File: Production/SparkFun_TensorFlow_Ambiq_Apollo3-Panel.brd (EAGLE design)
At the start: 162.4 x 134.7 mm, 1077 parts, among them J14 CORTEX_DEBUG_PTH, J15 CAMERA-0V7670, J20 CORTEX_DEBUG_PTH, J21 CAMERA-0V7670, J26 CORTEX_DEBUG_PTH, J27 CAMERA-0V7670, J32 CORTEX_DEBUG_PTH, J33 CAMERA-0V7670, J38 CORTEX_DEBUG_PTH, J39 CAMERA-0V7670, J44 CORTEX_DEBUG_PTH, J45 CAMERA-0V7670, J5 CORTEX_DEBUG_PTH, J50 CORTEX_DEBUG_PTH, J51 CAMERA-0V7670, J6 CAMERA-0V7670, J8 CORTEX_DEBUG_PTH, J9 CAMERA-0V7670, M1 MEMS_MIC, M10 MEMS_MIC, M11 MEMS_MIC, M12 MEMS_MIC, M13 MEMS_MIC, M14 MEMS_MIC, M15 MEMS_MIC, M16 MEMS_MIC, M17 MEMS_MIC, M18 MEMS_MIC, M2 MEMS_MIC, M3 MEMS_MIC, M4 MEMS_MIC, M5 MEMS_MIC, M6 MEMS_MIC, M7 MEMS_MIC, M8 MEMS_MIC, M9 MEMS_MIC, U1 AMBIQ-APOLLO3KBR, U10 LIS2DH12, U11 1.8V, U12 LMV358, U13 AMBIQ-APOLLO3KBR, U14 LIS2DH12, U15 1.8V, U16 LMV358, U17 AMBIQ-APOLLO3KBR, U18 LIS2DH12, U19 1.8V, U2 LIS2DH12, U20 LMV358, U21 AMBIQ-APOLLO3KBR, U22 LIS2DH12, U23 1.8V, U24 LMV358, U25 AMBIQ-APOLLO3KBR, U26 LIS2DH12, U27 1.8V, U28 LMV358, U29 AMBIQ-APOLLO3KBR, U3 1.8V, U30 LIS2DH12, U31 1.8V, U32 LMV358, U33 AMBIQ-APOLLO3KBR, U34 LIS2DH12, U35 1.8V, U36 LMV358, U4 LMV358, U5 AMBIQ-APOLLO3KBR, U6 LIS2DH12, U7 1.8V, U8 LMV358, U9 AMBIQ-APOLLO3KBR, Y1 32MHz, Y10 32.768kHz, Y11 32MHz, Y12 32.768kHz, Y13 32MHz, Y14 32.768kHz, Y15 32MHz, Y16 32.768kHz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

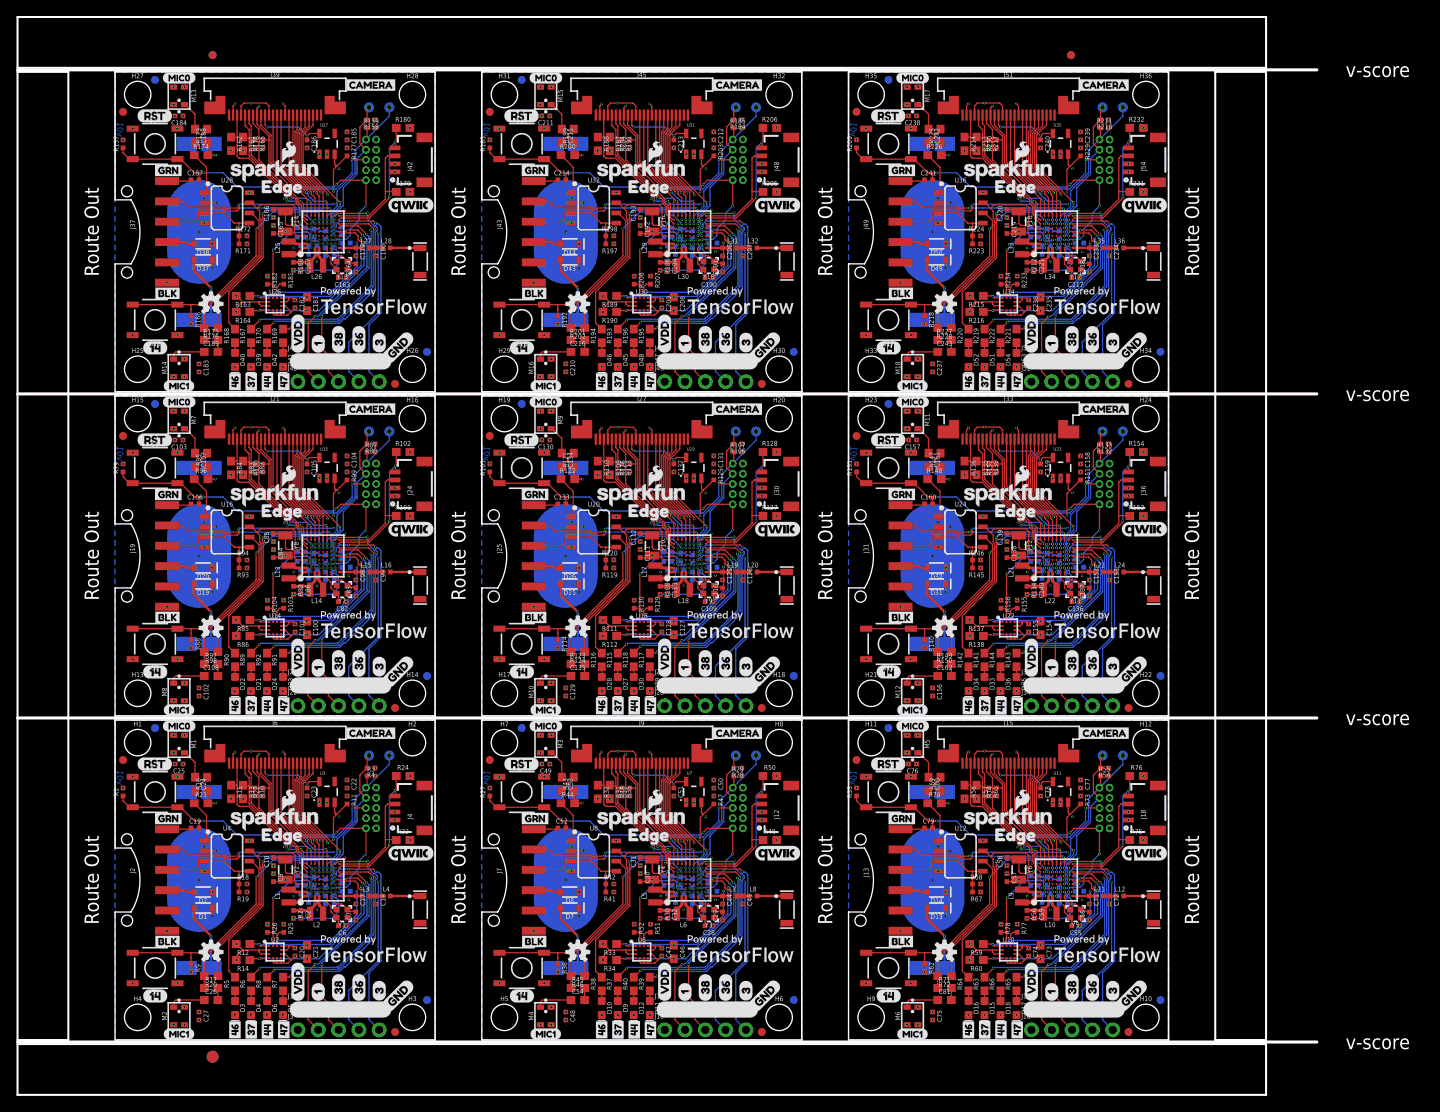
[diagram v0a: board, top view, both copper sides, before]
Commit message: Adding v01 Production panel.
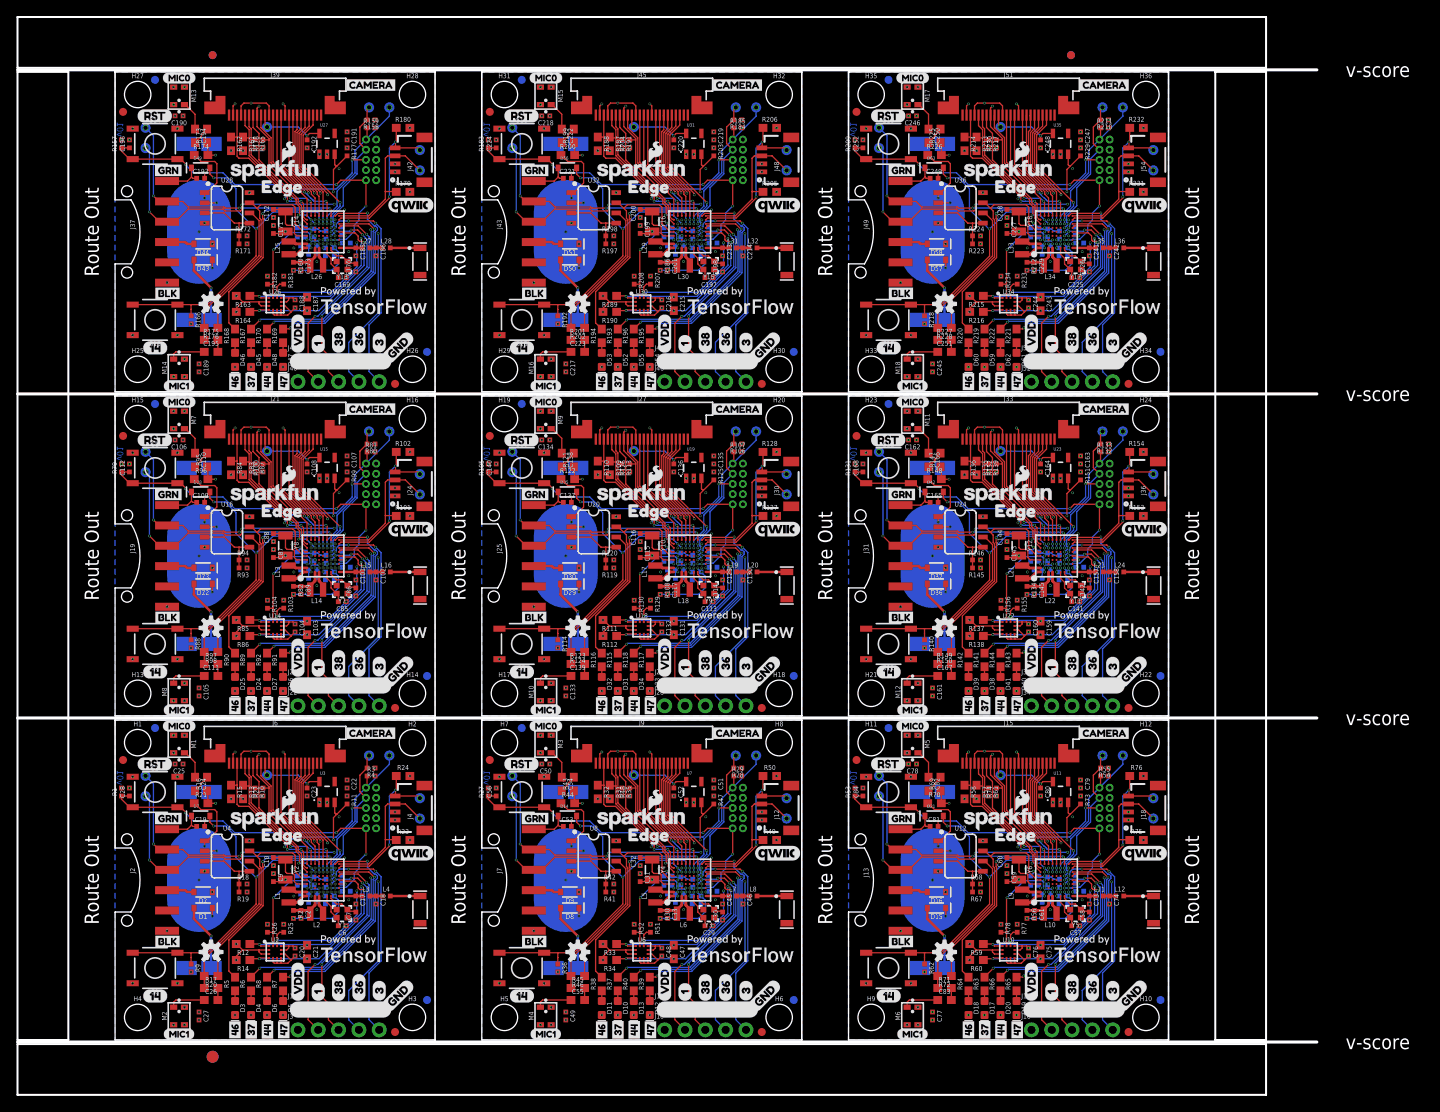
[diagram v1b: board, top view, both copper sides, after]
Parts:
- added C244, C245, C246, C249: 0.1uF, ambiq:0402-TIGHT
- added C247, C248: 1.0uF, ambiq:0402-TIGHT
- added C250, C251: 4.7uF, SparkFun-Capacitors:0603
- added C252: 1.0nF, ambiq:0402-TIGHT
- added D55, D62: GREEN, SparkFun-LED:LED-0603
- added D56, D63: 250mA/100V, SparkFun-DiscreteSemi:SOD-323
- added D57, D58: 1A/23V/620mV, SparkFun-DiscreteSemi:SOD-323@1
- added D59: BLUE, SparkFun-LED:LED-0603
- added D60: RED, SparkFun-LED:LED-0603
- added D61: Yellow, SparkFun-LED:LED-0603
- added TP19, TP20, TP21, TP22, TP23, TP24, TP25, TP26, TP27, TP28, TP29, TP30, TP31, TP32, TP33, TP34, TP35, TP36, TP37, TP38, TP39, TP40, TP41, TP42, TP43, TP44, TP45, TP46, TP47, TP48, TP49, TP50, TP51, TP52, TP53, TP54, TP55, TP56, TP57, TP58, TP59, TP60, TP61, TP62, TP63: TEST-POINT3X5, SparkFun-Connectors:PAD.03X.05
- added U$235, U$265: (no value), buzzard_labels:MIC00
- added U$236, U$266: (no value), buzzard_labels:MIC11
- added U$237, U$264, U$267: (no value), buzzard_labels:EDGE0
- added U$238, U$263, U$268: (no value), PoweredBy_TF#jpg:POWEREDBY_TF#JPG
- added U$239, U$269: (no value), SparkFun-Aesthetics:SFE_LOGO_NAME_.1
- added U$240, U$270: (no value), SparkFun-Aesthetics:OSHW-LOGO-S
- added U$241, U$248: (no value), buzzard_labels:GND0
- added U$242, U$245: (no value), buzzard_labels:VDD1
- added U$243, U$246: (no value), buzzard_labels:383
- added U$244, U$247: (no value), buzzard_labels:364
- added U$249: (no value), buzzard_labels:1416
- added U$250: (no value), buzzard_labels:RST15
- added U$251: (no value), buzzard_labels:BLK2
- added U$252: (no value), buzzard_labels:GRN1
- added U$253, U$254: (no value), buzzard_labels:10
- added U$255, U$256: (no value), buzzard_labels:31
- added U$257: (no value), buzzard_labels:461
- added U$258: (no value), buzzard_labels:372
- added U$259: (no value), buzzard_labels:443
- added U$260: (no value), buzzard_labels:470
- added U$261: (no value), Labels:QWIIC_COPYRIGHT_SMALL
- added U$262: (no value), buzzard_labels:CAMERA3
- BT1, BT2, BT3, BT4, BT5, BT6, BT7, BT8, BT9: device SparkFun-Batteries:BATTCON_20MM_4LEGS_OVERPASTE -> SparkFun-Batteries:BATTCON_20MM_4LEGS_OVERPASTE_INNER
- C100: value 10uF -> 2.2uF; device SparkFun-Capacitors:0603 -> ambiq:0402-TIGHT
- C101, C129, C157, C241: value 0.1uF -> DNP
- C102, C130, C214, C74: value 0.1uF -> 0.5pF
- C103, C187, C47, C75: value 0.1uF -> 10uF; device ambiq:0402-TIGHT -> SparkFun-Capacitors:0603
- C104, C105, C132, C50, C77, C78: value 1.0uF -> 0.1uF
- C107, C108, C135, C80: value 4.7uF -> 1.0uF; device SparkFun-Capacitors:0603 -> ambiq:0402-TIGHT
- C109, C137, C190, C217, C218: value 6pF -> 0.1uF
- C110, C55, C82, C83: value 6pF -> 4.7uF; device ambiq:0402-TIGHT -> SparkFun-Capacitors:0603
- C111, C138, C139, C166: value 15pF -> 4.7uF; device ambiq:0402-TIGHT -> SparkFun-Capacitors:0603
- C112, C84: value 15pF -> 1.0nF
- C113, C86: value 4.7uF -> 6pF
- C114, C141: value 1.0uF -> 6pF
- C115, C88: value 0.47uF -> 15pF
- C116, C143, C144, C171, C172, C199: value 2.2uF -> 15pF
- C117, C145, C89: value 2.2uF -> 4.7uF
- C118, C124, C151, C62, C70, C90, C97: value 2.2uF -> 1.0uF
- C119, C147, C175, C203: value 1.0uF -> 0.47uF
- C120, C121, C122, C148, C149, C176, C212, C240, C38, C65, C66, C92, C93, C94: value 1.0uF -> 2.2uF
- C123, C42, C69, C96: value 47nF -> 1.0uF
- C125, C152, C179, C98: value DNP -> 1.0uF
- C126, C153, C180, C207: value 0.5pF -> 1.0uF
- C127: value 10uF -> 47nF; device SparkFun-Capacitors:0603 -> ambiq:0402-TIGHT
- C128, C156, C184: value 0.1uF -> 2.2uF
- C131, C159: value 1.0uF -> 10uF; device ambiq:0402-TIGHT -> SparkFun-Capacitors:0603
- C134, C161, C162, C188, C189, C216, C53, C81: value 4.7uF -> 0.1uF; device SparkFun-Capacitors:0603 -> ambiq:0402-TIGHT
- C136, C163, C164, C191: value 6pF -> 1.0uF
- C140: value 4.7uF -> 1.0nF
- C142, C169: value 0.47uF -> 6pF
- C150, C177, C204: value 47nF -> 2.2uF
- C154, C181, C208, C235: value 10uF -> 1.0uF; device SparkFun-Capacitors:0603 -> ambiq:0402-TIGHT
- C155, C183, C211: value 0.1uF -> 47nF
- C158, C186: value 1.0uF -> 0.5pF
- C165, C193: value 15pF -> 0.1uF
- C167, C194: device ambiq:0402-TIGHT -> SparkFun-Capacitors:0603
- C168: value 1.0uF -> 1.0nF
- C170, C197, C198, C225, C226: value 2.2uF -> 6pF
- C173, C201, C229, C33: value 1.0uF -> 4.7uF
- C182, C209, C210, C236, C237, C238, C52, C79: value 0.1uF -> 1.0uF
- C185, C213: value 1.0uF -> DNP
- C192, C219, C220: value 15pF -> 1.0uF
- C195, C222: value 1.0uF -> 4.7uF; device ambiq:0402-TIGHT -> SparkFun-Capacitors:0603
- C196: value 0.47uF -> 1.0nF
- C200, C227, C228, C60, C87: value 1.0uF -> 15pF
- C206, C233, C44: value DNP -> 2.2uF
- C215, C243: value 4.7uF -> 10uF
- C221: value 4.7uF -> 0.1uF
- C223: value 0.47uF -> 4.7uF; device ambiq:0402-TIGHT -> SparkFun-Capacitors:0603
- C224: value 2.2uF -> 1.0nF
- C231: value 47nF -> 0.47uF
- C234, C72: value 0.5pF -> 2.2uF
- C239: value 1.0uF -> 47nF
- C242: value 4.7uF -> 0.5pF; device SparkFun-Capacitors:0603 -> ambiq:0402-TIGHT
- C28, C56: value 6pF -> 1.0nF
- C30, C57, C58, C85: value 15pF -> 6pF
- C32, C59: value 4.7uF -> 15pF
- C34: value 0.47uF -> 1.0uF
- C35, C63, C91: value 2.2uF -> 0.47uF
- C43: value 2.2uF -> 47nF
- C45: value 0.5pF -> DNP
- C46: value 10uF -> 0.5pF; device SparkFun-Capacitors:0603 -> ambiq:0402-TIGHT
- C61: value 0.47uF -> 4.7uF
- C71: value DNP -> 47nF
- C73: value 10uF -> DNP; device SparkFun-Capacitors:0603 -> ambiq:0402-TIGHT
- C99: value 0.5pF -> 47nF
- D1, D2, D37, D43, D44, D50, D8: device SparkFun-DiscreteSemi:SOD-323 -> SparkFun-DiscreteSemi:SOD-323@1
- D10, D52: value RED -> BLUE
- D11, D53: value Yellow -> RED
- D12, D54: value GREEN -> Yellow
- D13, D20: value 1A/23V/620mV -> GREEN; device SparkFun-DiscreteSemi:SOD-323 -> SparkFun-LED:LED-0603
- D14, D49, D7: value 1A/23V/620mV -> 250mA/100V
- D15, D51, D9: value BLUE -> 1A/23V/620mV; device SparkFun-LED:LED-0603 -> SparkFun-DiscreteSemi:SOD-323@1
- D16, D22: value RED -> 1A/23V/620mV; device SparkFun-LED:LED-0603 -> SparkFun-DiscreteSemi:SOD-323@1
- D17: value Yellow -> BLUE
- D18: value GREEN -> RED
- D19, D26: value 1A/23V/620mV -> Yellow; device SparkFun-DiscreteSemi:SOD-323 -> SparkFun-LED:LED-0603
- D21: value BLUE -> 250mA/100V; device SparkFun-LED:LED-0603 -> SparkFun-DiscreteSemi:SOD-323
- D23, D29: value Yellow -> 1A/23V/620mV; device SparkFun-LED:LED-0603 -> SparkFun-DiscreteSemi:SOD-323@1
- D24: value GREEN -> BLUE
- D25, D32: value 1A/23V/620mV -> RED; device SparkFun-DiscreteSemi:SOD-323 -> SparkFun-LED:LED-0603
- D27: value BLUE -> GREEN
- D28: value RED -> 250mA/100V; device SparkFun-LED:LED-0603 -> SparkFun-DiscreteSemi:SOD-323
- D30, D36: value GREEN -> 1A/23V/620mV; device SparkFun-LED:LED-0603 -> SparkFun-DiscreteSemi:SOD-323@1
- D31, D38: value 1A/23V/620mV -> BLUE; device SparkFun-DiscreteSemi:SOD-323 -> SparkFun-LED:LED-0603
- D33: value BLUE -> Yellow
- D34: value RED -> GREEN
- D35: value Yellow -> 250mA/100V; device SparkFun-LED:LED-0603 -> SparkFun-DiscreteSemi:SOD-323
- D39: value BLUE -> RED
- D40: value RED -> Yellow
- D41: value Yellow -> GREEN
- D42: value GREEN -> 250mA/100V; device SparkFun-LED:LED-0603 -> SparkFun-DiscreteSemi:SOD-323
- R120, R146, R172, R18, R198, R224, R42, R68, R94: value 10k -> 22k
- U$100: device buzzard_labels:CAMERA3 -> buzzard_labels:RST15
- U$101: device PoweredBy_TF#jpg:POWEREDBY_TF#JPG -> buzzard_labels:BLK2
- U$102: device buzzard_labels:EDGE0 -> buzzard_labels:GRN1
- U$103: device buzzard_labels:MIC00 -> buzzard_labels:10
- U$104: device buzzard_labels:MIC11 -> buzzard_labels:10
- U$105: device buzzard_labels:GND0 -> buzzard_labels:31
- U$106, U$135: device buzzard_labels:VDD1 -> buzzard_labels:31
- U$107: device buzzard_labels:383 -> buzzard_labels:461
- U$108: device buzzard_labels:364 -> buzzard_labels:372
- U$109: device buzzard_labels:VDD1 -> buzzard_labels:443
- U$110: device buzzard_labels:383 -> buzzard_labels:470
- U$111: device buzzard_labels:364 -> Labels:QWIIC_COPYRIGHT_SMALL
- U$112: device buzzard_labels:GND0 -> buzzard_labels:CAMERA3
- U$113: device buzzard_labels:1416 -> PoweredBy_TF#jpg:POWEREDBY_TF#JPG
- U$114: device buzzard_labels:RST15 -> buzzard_labels:EDGE0
- U$115: device buzzard_labels:BLK2 -> buzzard_labels:MIC00
- U$116: device buzzard_labels:GRN1 -> buzzard_labels:MIC11
- U$117, U$144: device buzzard_labels:10 -> buzzard_labels:EDGE0
- U$118, U$143: device buzzard_labels:10 -> PoweredBy_TF#jpg:POWEREDBY_TF#JPG
- U$119: device buzzard_labels:31 -> SparkFun-Aesthetics:SFE_LOGO_NAME_.1
- U$120: device buzzard_labels:31 -> SparkFun-Aesthetics:OSHW-LOGO-S
- U$121: device buzzard_labels:461 -> buzzard_labels:GND0
- U$122: device buzzard_labels:372 -> buzzard_labels:VDD1
- U$123: device buzzard_labels:443 -> buzzard_labels:383
- U$124: device buzzard_labels:470 -> buzzard_labels:364
- U$125: device Labels:QWIIC_COPYRIGHT_SMALL -> buzzard_labels:VDD1
- U$126: device buzzard_labels:CAMERA3 -> buzzard_labels:383
- U$127: device PoweredBy_TF#jpg:POWEREDBY_TF#JPG -> buzzard_labels:364
- U$128: device buzzard_labels:EDGE0 -> buzzard_labels:GND0
- U$129: device buzzard_labels:MIC00 -> buzzard_labels:1416
- U$130: device buzzard_labels:MIC11 -> buzzard_labels:RST15
- U$131: device buzzard_labels:GND0 -> buzzard_labels:BLK2
- U$132: device buzzard_labels:VDD1 -> buzzard_labels:GRN1
- U$133: device buzzard_labels:383 -> buzzard_labels:10
- U$134, U$163: device buzzard_labels:364 -> buzzard_labels:10
- U$136: device buzzard_labels:383 -> buzzard_labels:31
- U$137: device buzzard_labels:364 -> buzzard_labels:461
- U$138: device buzzard_labels:GND0 -> buzzard_labels:372
- U$139: device buzzard_labels:1416 -> buzzard_labels:443
- U$140: device buzzard_labels:RST15 -> buzzard_labels:470
- U$141: device buzzard_labels:BLK2 -> Labels:QWIIC_COPYRIGHT_SMALL
- U$142: device buzzard_labels:GRN1 -> buzzard_labels:CAMERA3
- U$145: device buzzard_labels:31 -> buzzard_labels:MIC00
- U$146: device buzzard_labels:31 -> buzzard_labels:MIC11
- U$147: device buzzard_labels:461 -> buzzard_labels:EDGE0
- U$148: device buzzard_labels:372 -> PoweredBy_TF#jpg:POWEREDBY_TF#JPG
- U$149: device buzzard_labels:443 -> SparkFun-Aesthetics:SFE_LOGO_NAME_.1
- U$150: device buzzard_labels:470 -> SparkFun-Aesthetics:OSHW-LOGO-S
- U$151: device Labels:QWIIC_COPYRIGHT_SMALL -> buzzard_labels:GND0
- U$152: device buzzard_labels:CAMERA3 -> buzzard_labels:VDD1
- U$153: device PoweredBy_TF#jpg:POWEREDBY_TF#JPG -> buzzard_labels:383
- U$154: device buzzard_labels:EDGE0 -> buzzard_labels:364
- U$155: device buzzard_labels:MIC00 -> buzzard_labels:VDD1
- U$156: device buzzard_labels:MIC11 -> buzzard_labels:383
- U$157, U$34: device buzzard_labels:GND0 -> buzzard_labels:364
- U$158, U$31: device buzzard_labels:VDD1 -> buzzard_labels:GND0
- U$159: device buzzard_labels:383 -> buzzard_labels:1416
- U$160: device buzzard_labels:364 -> buzzard_labels:RST15
- U$161: device buzzard_labels:VDD1 -> buzzard_labels:BLK2
- U$162: device buzzard_labels:383 -> buzzard_labels:GRN1
- U$164: device buzzard_labels:GND0 -> buzzard_labels:10
- U$165: device buzzard_labels:1416 -> buzzard_labels:31
- U$166: device buzzard_labels:RST15 -> buzzard_labels:31
- U$167: device buzzard_labels:BLK2 -> buzzard_labels:461
- U$168: device buzzard_labels:GRN1 -> buzzard_labels:372
- U$169: device buzzard_labels:10 -> buzzard_labels:443
- U$170: device buzzard_labels:10 -> buzzard_labels:470
- U$171: device buzzard_labels:31 -> Labels:QWIIC_COPYRIGHT_SMALL
- U$172: device buzzard_labels:31 -> buzzard_labels:CAMERA3
- U$173: device buzzard_labels:461 -> PoweredBy_TF#jpg:POWEREDBY_TF#JPG
- U$174: device buzzard_labels:372 -> buzzard_labels:EDGE0
- U$175: device buzzard_labels:443 -> buzzard_labels:MIC00
- U$176: device buzzard_labels:470 -> buzzard_labels:MIC11
- U$177: device Labels:QWIIC_COPYRIGHT_SMALL -> buzzard_labels:EDGE0
- U$178: device buzzard_labels:CAMERA3 -> PoweredBy_TF#jpg:POWEREDBY_TF#JPG
- U$179: device PoweredBy_TF#jpg:POWEREDBY_TF#JPG -> SparkFun-Aesthetics:SFE_LOGO_NAME_.1
- U$180: device buzzard_labels:EDGE0 -> SparkFun-Aesthetics:OSHW-LOGO-S
- U$181: device buzzard_labels:MIC00 -> buzzard_labels:GND0
- U$182: device buzzard_labels:MIC11 -> buzzard_labels:VDD1
- U$183, U$216: device buzzard_labels:GND0 -> buzzard_labels:383
- U$184, U$187: device buzzard_labels:VDD1 -> buzzard_labels:364
- U$185, U$32: device buzzard_labels:383 -> buzzard_labels:VDD1
- U$186, U$33: device buzzard_labels:364 -> buzzard_labels:383
- U$188, U$211: device buzzard_labels:383 -> buzzard_labels:GND0
- U$189: device buzzard_labels:364 -> buzzard_labels:1416
- U$190: device buzzard_labels:GND0 -> buzzard_labels:RST15
- U$191: device buzzard_labels:1416 -> buzzard_labels:BLK2
- U$192: device buzzard_labels:RST15 -> buzzard_labels:GRN1
- U$193: device buzzard_labels:BLK2 -> buzzard_labels:10
- U$194: device buzzard_labels:GRN1 -> buzzard_labels:10
- U$195, U$196: device buzzard_labels:10 -> buzzard_labels:31
- U$197: device buzzard_labels:31 -> buzzard_labels:461
- U$198: device buzzard_labels:31 -> buzzard_labels:372
- U$199: device buzzard_labels:461 -> buzzard_labels:443
- U$200: device buzzard_labels:372 -> buzzard_labels:470
- U$201: device buzzard_labels:443 -> Labels:QWIIC_COPYRIGHT_SMALL
- U$202: device buzzard_labels:470 -> buzzard_labels:CAMERA3
- U$203: device Labels:QWIIC_COPYRIGHT_SMALL -> PoweredBy_TF#jpg:POWEREDBY_TF#JPG
- U$204: device buzzard_labels:CAMERA3 -> buzzard_labels:EDGE0
- U$205: device PoweredBy_TF#jpg:POWEREDBY_TF#JPG -> buzzard_labels:MIC00
- U$206: device buzzard_labels:EDGE0 -> buzzard_labels:MIC11
- U$207: device buzzard_labels:MIC00 -> buzzard_labels:EDGE0
- U$208: device buzzard_labels:MIC11 -> PoweredBy_TF#jpg:POWEREDBY_TF#JPG
- U$209: device buzzard_labels:GND0 -> SparkFun-Aesthetics:SFE_LOGO_NAME_.1
- U$210: device buzzard_labels:VDD1 -> SparkFun-Aesthetics:OSHW-LOGO-S
- U$212, U$215: device buzzard_labels:364 -> buzzard_labels:VDD1
- U$213: device buzzard_labels:VDD1 -> buzzard_labels:383
- U$214: device buzzard_labels:383 -> buzzard_labels:364
- U$217: device buzzard_labels:1416 -> buzzard_labels:364
- U$218: device buzzard_labels:RST15 -> buzzard_labels:GND0
- U$219: device buzzard_labels:BLK2 -> buzzard_labels:1416
- U$220: device buzzard_labels:GRN1 -> buzzard_labels:RST15
- U$221: device buzzard_labels:10 -> buzzard_labels:BLK2
- U$222: device buzzard_labels:10 -> buzzard_labels:GRN1
- U$223, U$224: device buzzard_labels:31 -> buzzard_labels:10
- U$225: device buzzard_labels:461 -> buzzard_labels:31
- U$226: device buzzard_labels:372 -> buzzard_labels:31
- U$227: device buzzard_labels:443 -> buzzard_labels:461
- U$228: device buzzard_labels:470 -> buzzard_labels:372
- U$229: device Labels:QWIIC_COPYRIGHT_SMALL -> buzzard_labels:443
- U$23: device buzzard_labels:GND0 -> buzzard_labels:EDGE0
- U$230: device buzzard_labels:CAMERA3 -> buzzard_labels:470
- U$231: device PoweredBy_TF#jpg:POWEREDBY_TF#JPG -> Labels:QWIIC_COPYRIGHT_SMALL
- U$232: device buzzard_labels:EDGE0 -> buzzard_labels:CAMERA3
- U$233: device buzzard_labels:MIC00 -> PoweredBy_TF#jpg:POWEREDBY_TF#JPG
- U$234: device buzzard_labels:MIC11 -> buzzard_labels:EDGE0
- U$25, U$83: device buzzard_labels:VDD1 -> PoweredBy_TF#jpg:POWEREDBY_TF#JPG
- U$29: device buzzard_labels:383 -> SparkFun-Aesthetics:SFE_LOGO_NAME_.1
- U$30: device buzzard_labels:364 -> SparkFun-Aesthetics:OSHW-LOGO-S
- U$35: device buzzard_labels:1416 -> buzzard_labels:VDD1
- U$36: device buzzard_labels:RST15 -> buzzard_labels:383
- U$37: device buzzard_labels:BLK2 -> buzzard_labels:364
- U$38: device buzzard_labels:GRN1 -> buzzard_labels:GND0
- U$39: device buzzard_labels:10 -> buzzard_labels:1416
- U$40: device buzzard_labels:10 -> buzzard_labels:RST15
- U$41: device buzzard_labels:31 -> buzzard_labels:BLK2
- U$42: device buzzard_labels:31 -> buzzard_labels:GRN1
- U$43: device buzzard_labels:461 -> buzzard_labels:10
- U$44: device buzzard_labels:372 -> buzzard_labels:10
- U$45: device buzzard_labels:443 -> buzzard_labels:31
- U$46: device buzzard_labels:470 -> buzzard_labels:31
- U$47: device Labels:QWIIC_COPYRIGHT_SMALL -> buzzard_labels:461
- U$48: device buzzard_labels:CAMERA3 -> buzzard_labels:372
- U$49: device PoweredBy_TF#jpg:POWEREDBY_TF#JPG -> buzzard_labels:443
- U$50: device buzzard_labels:EDGE0 -> buzzard_labels:470
- U$51: device buzzard_labels:MIC00 -> Labels:QWIIC_COPYRIGHT_SMALL
- U$52: device buzzard_labels:MIC11 -> buzzard_labels:CAMERA3
- U$53: device buzzard_labels:GND0 -> PoweredBy_TF#jpg:POWEREDBY_TF#JPG
- U$54, U$57: device buzzard_labels:VDD1 -> buzzard_labels:EDGE0
- U$55: device buzzard_labels:383 -> buzzard_labels:MIC00
- U$56: device buzzard_labels:364 -> buzzard_labels:MIC11
- U$58: device buzzard_labels:383 -> PoweredBy_TF#jpg:POWEREDBY_TF#JPG
- U$59: device buzzard_labels:364 -> SparkFun-Aesthetics:SFE_LOGO_NAME_.1
- U$60: device buzzard_labels:GND0 -> SparkFun-Aesthetics:OSHW-LOGO-S
- U$61: device buzzard_labels:1416 -> buzzard_labels:GND0
- U$62: device buzzard_labels:RST15 -> buzzard_labels:VDD1
- U$63: device buzzard_labels:BLK2 -> buzzard_labels:383
- U$64: device buzzard_labels:GRN1 -> buzzard_labels:364
- U$65, U$92: device buzzard_labels:10 -> buzzard_labels:VDD1
- U$66: device buzzard_labels:10 -> buzzard_labels:383
- U$67, U$94: device buzzard_labels:31 -> buzzard_labels:364
- U$68: device buzzard_labels:31 -> buzzard_labels:GND0
- U$69: device buzzard_labels:461 -> buzzard_labels:1416
- U$70: device buzzard_labels:372 -> buzzard_labels:RST15
- U$71: device buzzard_labels:443 -> buzzard_labels:BLK2
- U$72: device buzzard_labels:470 -> buzzard_labels:GRN1
- U$73: device Labels:QWIIC_COPYRIGHT_SMALL -> buzzard_labels:10
- U$74: device buzzard_labels:CAMERA3 -> buzzard_labels:10
- U$75: device PoweredBy_TF#jpg:POWEREDBY_TF#JPG -> buzzard_labels:31
- U$76: device buzzard_labels:EDGE0 -> buzzard_labels:31
- U$77: device buzzard_labels:MIC00 -> buzzard_labels:461
- U$78: device buzzard_labels:MIC11 -> buzzard_labels:372
- U$79: device buzzard_labels:GND0 -> buzzard_labels:443
- U$80: device buzzard_labels:VDD1 -> buzzard_labels:470
- U$81: device buzzard_labels:383 -> Labels:QWIIC_COPYRIGHT_SMALL
- U$82: device buzzard_labels:364 -> buzzard_labels:CAMERA3
- U$84: device buzzard_labels:383 -> buzzard_labels:EDGE0
- U$85: device buzzard_labels:364 -> buzzard_labels:MIC00
- U$86: device buzzard_labels:GND0 -> buzzard_labels:MIC11
- U$87: device buzzard_labels:1416 -> buzzard_labels:EDGE0
- U$88: device buzzard_labels:RST15 -> PoweredBy_TF#jpg:POWEREDBY_TF#JPG
- U$89: device buzzard_labels:BLK2 -> SparkFun-Aesthetics:SFE_LOGO_NAME_.1
- U$90: device buzzard_labels:GRN1 -> SparkFun-Aesthetics:OSHW-LOGO-S
- U$91: device buzzard_labels:10 -> buzzard_labels:GND0
- U$93: device buzzard_labels:31 -> buzzard_labels:383
- U$95: device buzzard_labels:461 -> buzzard_labels:VDD1
- U$96: device buzzard_labels:372 -> buzzard_labels:383
- U$97: device buzzard_labels:443 -> buzzard_labels:364
- U$98: device buzzard_labels:470 -> buzzard_labels:GND0
- U$99: device Labels:QWIIC_COPYRIGHT_SMALL -> buzzard_labels:1416
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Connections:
- removed net N$100 (its old number): C190.2, U29.F1, Y15.3
- removed net N$103 (its old number): C214.1, J43.1
- removed net N$113 (its old number): C218.2, U33.G1, Y17.1
- removed net N$115 (its old number): C234.1, L35.2, L36.1
- removed net N$118: D51.A, R219.1
- removed net N$119: D52.A, R220.1
- removed net N$120: D53.A, R221.1
- removed net N$121: D54.A, R222.1
- removed net N$123: C242.2, R225.2
- removed net N$126: C243.2, R227.2
- removed net N$17 (its old number): C45.1, L7.2, L8.1
- removed net N$22 (its old number): D11.A, R39.1
- removed net N$25 (its old number): C53.2, R43.2
- removed net N$30 (its old number): C55.2, U9.F1, Y5.3
- removed net N$35 (its old number): D16.A, R64.1
- removed net N$37 (its old number): D18.A, R66.1
- removed net N$43 (its old number): C83.2, U13.G1, Y7.1
- removed net N$48 (its old number): D21.A, R89.1
- removed net N$50 (its old number): D23.A, R91.1
- removed net N$51 (its old number): D24.A, R92.1
- removed net N$56 (its old number): C108.2, R97.2
- removed net N$61 (its old number): C133.1, J25.1
- removed net N$63 (its old number): D28.A, R116.1
- removed net N$64 (its old number): D29.A, R117.1
- removed net N$76 (its old number): D33.A, R141.1
- removed net N$77 (its old number): D34.A, R142.1
- removed net N$87 (its old number): C180.1, L27.2, L28.1
- removed net N$89 (its old number): C187.1, J37.1
- removed net N$90 (its old number): D39.A, R167.1
- removed net N$95 (its old number): C188.2, R173.2
- new net DTR: C19.1, D7.C, J2.1
- new net DTR1: C53.1, D14.C, J7.1
- new net DTR2: C81.1, D21.C, J13.1
- new net DTR3: C109.1, D28.C, J19.1
- new net DTR4: C137.1, D35.C, J25.1
- new net DTR5: C165.1, D42.C, J31.1
- new net DTR6: C193.1, D49.C, J37.1
- new net DTR7: C221.1, D56.C, J43.1
- new net DTR8: C249.1, D63.C, J49.1
- new net DVDD: C11.1, U1.H3
- new net DVDD1: C43.1, U5.H3
- new net DVDD2: C71.1, U9.H3
- new net DVDD3: C99.1, U13.H3
- new net DVDD4: C127.1, U17.H3
- new net DVDD5: C155.1, U21.H3
- new net DVDD6: C183.1, U25.H3
- new net DVDD7: C211.1, U29.H3
- new net DVDD8: C239.1, U33.H3
- new net N$110: D60.A, R220.1
- new net N$111: D61.A, R221.1
- new net N$18: D10.A, R37.1
- new net N$26: C55.2, R45.2
- new net N$27: C58.2, U9.G1, Y5.1
- new net N$32: D18.A, R64.1
- new net N$40: C86.2, U13.G1, Y7.1
- new net N$41: C85.2, U13.F1, Y7.3
- new net N$46: D26.A, R91.1
- new net N$52: C111.2, R97.2
- new net N$54: C113.2, U17.F1, Y9.3
- new net N$55: C130.1, L19.2, L20.1
- new net N$60: D34.A, R118.1
- new net N$66: C142.2, U21.G1, Y11.1
- new net N$68: C158.1, L23.2, L24.1
- new net N$80: C169.2, U25.F1, Y13.3
- new net N$83: D45.A, R167.1
- new net N$88: C194.2, R173.2
- new net N$94: C214.1, L31.2, L32.1
- new net N$96: D52.A, R193.1
- new net N$97: D53.A, R194.1
- net 1.8V: now also TP7.P$1
- net 1.8V1: now also C52.1, TP14.P$1; no longer C51.1
- net 1.8V2: now also C80.1, TP21.P$1; no longer C78.1
- net 1.8V3: now also C108.1, TP28.P$1; no longer C105.1
- net 1.8V4: now also C136.1, TP35.P$1; no longer C132.1
- net 1.8V5: now also C164.1, TP42.P$1; no longer C159.1
- net 1.8V6: now also C192.1, TP49.P$1; no longer C186.1
- net 1.8V7: now also C220.1, TP56.P$1; no longer C213.1
- net 1.8V8: now also C248.1, TP63.P$1; no longer C240.1
- net ADC_VREF1: now also C35.1; no longer C34.1
- net ADC_VREF2: now also C63.1; no longer C61.1
- net ADC_VREF3: now also C91.1; no longer C88.1
- net ADC_VREF4: now also C119.1; no longer C115.1
- net ADC_VREF5: now also C147.1; no longer C142.1
- net ADC_VREF6: now also C175.1; no longer C169.1
- net ADC_VREF7: now also C203.1; no longer C196.1
- net ADC_VREF8: now also C231.1; no longer C223.1
- net AMBIQ_!RST: now also C28.1
- net AMBIQ_!RST1: now also C53.2, C56.1; no longer C52.2
- net AMBIQ_!RST2: now also C81.2, C84.1; no longer C79.2
- net AMBIQ_!RST3: now also C109.2, C112.1; no longer C106.2
- net AMBIQ_!RST4: now also C137.2, C140.1; no longer C133.2
- net AMBIQ_!RST5: now also C165.2, C168.1; no longer C160.2
- net AMBIQ_!RST6: now also C193.2, C196.1; no longer C187.2
- net AMBIQ_!RST7: now also C221.2, C224.1; no longer C214.2
- net AMBIQ_!RST8: now also C249.2, C252.1; no longer C241.2
- net FTDI_VCC1: now also D9.A; no longer D8.A
- net FTDI_VCC2: now also D16.A; no longer D14.A
- net FTDI_VCC3: now also D23.A; no longer D20.A
- net FTDI_VCC4: now also D30.A; no longer D26.A
- net FTDI_VCC5: now also D37.A; no longer D32.A
- net FTDI_VCC6: now also D44.A; no longer D38.A
- net FTDI_VCC7: now also D51.A; no longer D44.A
- net FTDI_VCC8: now also D58.A; no longer D50.A
- net GND: now also C28.2
- net GND1: now also C32.1, C52.2, C56.2, D13.C; no longer C28.1, C32.2, D9.C
- net GND2: now also C59.1, C60.1, C79.2, C80.2, C84.2, D19.C, D20.C; no longer C55.1, C56.1, C59.2, C60.2, D15.C, D16.C
- net GND3: now also C106.2, C107.2, C108.2, C112.2, C86.1, C87.1, C88.1, D25.C, D26.C, D27.C; no longer C82.1, C83.1, C84.1, C86.2, C87.2, C88.2, D21.C, D22.C, D23.C
- net GND4: now also C113.1, C114.1, C115.1, C116.1, C133.2, C134.2, C135.2, C136.2, C140.2, D31.C, D32.C, D33.C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; no longer C109.1, C110.1, C111.1, C112.1, C113.2, C114.2, C115.2, C116.2, D27.C, D28.C, D29.C, D30.C
- net GND5: now also C141.1, C142.1, C143.1, C144.1, C160.2, C161.2, C162.2, C163.2, C164.2, C168.2, D38.C, D39.C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; no longer C136.1, C137.1, C138.1, C139.1, C140.2, C141.2, C142.2, C143.2, C144.2, D33.C, D34.C, D35.C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
- net GND6: now also C169.1, C170.1, C171.1, C172.1, C187.2, C188.2, C189.2, C190.2, C191.2, C192.2, C196.2, D45.C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; no longer C163.1, C164.1, C165.1, C166.1, C167.2, C168.2, C169.2, C170.2, C171.2, C172.2, D39.C, D40.C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
- net GND7: now also C197.1, C198.1, C199.1, C200.1, C214.2, C215.2, C216.2, C217.2, C218.2, C219.2, C220.2, C224.2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; no longer C190.1, C191.1, C192.1, C193.1, C194.2, C195.2, C196.2, C197.2, C198.2, C199.2, C200.2, D45.C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
- net GND8: now also C225.1, C226.1, C227.1, C228.1, C241.2, C242.2, C243.2, C244.2, C245.2, C246.2, C247.2, C248.2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; no longer C217.1, C218.1, C219.1, C220.1, C221.2, C222.2, C223.2, C224.2, C225.2, C226.2, C227.2, C228.2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
- net GPIO14/USER_BUTTON: now also D7.A
- net GPIO14/USER_BUTTON1: now also D14.A
- net GPIO14/USER_BUTTON2: now also D21.A
- net GPIO14/USER_BUTTON3: now also D28.A
- net GPIO14/USER_BUTTON4: now also D35.A
- net GPIO14/USER_BUTTON5: now also D42.A
- net GPIO14/USER_BUTTON6: now also D49.A
- net GPIO14/USER_BUTTON7: now also D56.A
- net GPIO14/USER_BUTTON8: now also D63.A
- net GPIO20/SWDCK1: now also TP8.P$1; no longer TP3.P$1
- net GPIO20/SWDCK2: now also TP15.P$1; no longer TP5.P$1
- net GPIO20/SWDCK3: now also TP22.P$1; no longer TP7.P$1
- net GPIO20/SWDCK4: now also TP29.P$1; no longer TP9.P$1
- net GPIO20/SWDCK5: now also TP36.P$1; no longer TP11.P$1
- net GPIO20/SWDCK6: now also TP43.P$1; no longer TP13.P$1
- net GPIO20/SWDCK7: now also TP50.P$1; no longer TP15.P$1
- net GPIO20/SWDCK8: now also TP57.P$1; no longer TP17.P$1
- net GPIO21/SWDIO1: now also TP9.P$1; no longer TP4.P$1
- net GPIO21/SWDIO2: now also TP16.P$1; no longer TP6.P$1
- net GPIO21/SWDIO3: now also TP23.P$1; no longer TP8.P$1
- net GPIO21/SWDIO4: now also TP30.P$1; no longer TP10.P$1
- net GPIO21/SWDIO5: now also TP37.P$1; no longer TP12.P$1
- net GPIO21/SWDIO6: now also TP44.P$1; no longer TP14.P$1
- net GPIO21/SWDIO7: now also TP51.P$1; no longer TP16.P$1
- net GPIO21/SWDIO8: now also TP58.P$1; no longer TP18.P$1
- net GPIO39_QWIIC_SCK: now also TP3.P$1
- net GPIO39_QWIIC_SCK1: now also TP10.P$1
- net GPIO39_QWIIC_SCK2: now also TP17.P$1
- net GPIO39_QWIIC_SCK3: now also TP24.P$1
- net GPIO39_QWIIC_SCK4: now also TP31.P$1
- net GPIO39_QWIIC_SCK5: now also TP38.P$1
- net GPIO39_QWIIC_SCK6: now also TP45.P$1
- net GPIO39_QWIIC_SCK7: now also TP52.P$1
- net GPIO39_QWIIC_SCK8: now also TP59.P$1
- net GPIO40_QWIIC_SDA: now also TP4.P$1
- net GPIO40_QWIIC_SDA1: now also TP11.P$1
- net GPIO40_QWIIC_SDA2: now also TP18.P$1
- net GPIO40_QWIIC_SDA3: now also TP25.P$1
- net GPIO40_QWIIC_SDA4: now also TP32.P$1
- net GPIO40_QWIIC_SDA5: now also TP39.P$1
- net GPIO40_QWIIC_SDA6: now also TP46.P$1
- net GPIO40_QWIIC_SDA7: now also TP53.P$1
- net GPIO40_QWIIC_SDA8: now also TP60.P$1
- net MIC0_OUT1: now also C54.1; no longer C53.1
- net MIC0_OUT2: now also C82.1; no longer C80.1
- net MIC0_OUT3: now also C110.1; no longer C107.1
- net MIC0_OUT4: now also C138.1; no longer C134.1
- net MIC0_OUT5: now also C166.1; no longer C161.1
- net MIC0_OUT6: now also C194.1; no longer C188.1
- net MIC0_OUT7: now also C222.1; no longer C215.1
- net MIC0_OUT8: now also C250.1; no longer C242.1
- net MIC1_OUT1: now also C55.1; no longer C54.1
- net MIC1_OUT2: now also C83.1; no longer C81.1
- net MIC1_OUT3: now also C111.1; no longer C108.1
- net MIC1_OUT4: now also C139.1; no longer C135.1
- net MIC1_OUT5: now also C167.1; no longer C162.1
- net MIC1_OUT6: now also C195.1; no longer C189.1
- net MIC1_OUT7: now also C223.1; no longer C216.1
- net MIC1_OUT8: now also C251.1; no longer C243.1
- net N$101: now also C222.2, R199.2; no longer C207.1, L31.2, L32.1
- net N$104: now also C223.2, R201.2; no longer D45.A, R193.1
- net N$105: now also C226.2, U33.G1, Y17.1; no longer D46.A, R194.1
- net N$106: now also C225.2, U33.F1, Y17.3; no longer D47.A, R195.1
- net N$107: now also C242.1, L35.2, L36.1; no longer D48.A, R196.1
- net N$109: now also D59.A, R219.1; no longer C215.2, R199.2
- net N$112: now also D62.A, R222.1; no longer C216.2, R201.2
- net N$114: now also C250.2, R225.2; no longer C217.2, U33.F1, Y17.3
- net N$117: now also C251.2, R227.2; no longer C241.1, J49.1
- net N$13: now also U5.F1, Y3.3; no longer U5.G1, Y3.1
- net N$15: now also C46.1, L7.2, L8.1; no longer C28.2, U5.F1, Y3.3
- net N$19: now also D11.A, R38.1; no longer C52.1, J7.1
- net N$20: now also D12.A, R39.1; no longer D9.A, R37.1
- net N$21: now also D13.A, R40.1; no longer D10.A, R38.1
- net N$23: now also C54.2, R43.2; no longer D12.A, R40.1
- net N$28: now also C57.2, U9.F1, Y5.3; no longer C54.2, R45.2
- net N$29: now also C74.1, L11.2, L12.1; no longer C56.2, U9.G1, Y5.1
- net N$31: now also D17.A, R63.1; no longer C72.1, L11.2, L12.1
- net N$33: now also D19.A, R65.1; no longer C79.1, J13.1
- net N$34: now also D20.A, R66.1; no longer D15.A, R63.1
- net N$36: now also C82.2, R69.2; no longer D17.A, R65.1
- net N$39: now also C83.2, R71.2; no longer C80.2, R69.2
- net N$4: now also C30.2, U5.G1, Y3.1; no longer C19.1, J2.1
- net N$42: now also C102.1, L15.2, L16.1; no longer C81.2, R71.2
- net N$44: now also D24.A, R89.1; no longer C82.2, U13.F1, Y7.3
- net N$45: now also D25.A, R90.1; no longer C99.1, L15.2, L16.1
- net N$47: now also D27.A, R92.1; no longer C106.1, J19.1
- net N$49: now also C110.2, R95.2; no longer D22.A, R90.1
- net N$53: now also C114.2, U17.G1, Y9.1; no longer C107.2, R95.2
- net N$57: now also D31.A, R115.1; no longer C110.2, U17.G1, Y9.1
- net N$58: now also D32.A, R116.1; no longer C109.2, U17.F1, Y9.3
- net N$59: now also D33.A, R117.1; no longer C126.1, L19.2, L20.1
- net N$62: now also C138.2, R121.2; no longer D27.A, R115.1
- net N$65: now also C139.2, R123.2; no longer D30.A, R118.1
- net N$67: now also C141.2, U21.F1, Y11.3; no longer C134.2, R121.2
- net N$70: now also D38.A, R141.1; no longer C135.2, R123.2
- net N$71: now also D39.A, R142.1; no longer C137.2, U21.G1, Y11.1
- net N$72: now also D40.A, R143.1; no longer C136.2, U21.F1, Y11.3
- net N$73: now also D41.A, R144.1; no longer C153.1, L23.2, L24.1
- net N$75: now also C166.2, R147.2; no longer C160.1, J31.1
- net N$78: now also C167.2, R149.2; no longer D35.A, R143.1
- net N$79: now also C170.2, U25.G1, Y13.1; no longer D36.A, R144.1
- net N$81: now also C186.1, L27.2, L28.1; no longer C161.2, R147.2
- net N$84: now also D46.A, R168.1; no longer C162.2, R149.2
- net N$85: now also D47.A, R169.1; no longer C164.2, U25.G1, Y13.1
- net N$86: now also D48.A, R170.1; no longer C163.2, U25.F1, Y13.3
- net N$91: now also C195.2, R175.2; no longer D40.A, R168.1
- net N$92: now also C198.2, U29.G1, Y15.1; no longer D41.A, R169.1
- net N$93: now also C197.2, U29.F1, Y15.3; no longer D42.A, R170.1
- net N$98: now also D54.A, R195.1; no longer C189.2, R175.2
- net N$99: now also D55.A, R196.1; no longer C191.2, U29.G1, Y15.1
- net RFIOP1: now also C45.1; no longer C44.1
- net RFIOP2: now also C73.1; no longer C71.1
- net RFIOP3: now also C101.1; no longer C98.1
- net RFIOP4: now also C129.1; no longer C125.1
- net RFIOP5: now also C157.1; no longer C152.1
- net RFIOP6: now also C185.1; no longer C179.1
- net RFIOP7: now also C213.1; no longer C206.1
- net RFIOP8: now also C241.1; no longer C233.1
- net UART-RX/GPIO1: now also TP13.P$1
- net UART-RX/GPIO2: now also TP20.P$1
- net UART-RX/GPIO3: now also TP27.P$1
- net UART-RX/GPIO4: now also TP34.P$1
- net UART-RX/GPIO49: now also TP6.P$1
- net UART-RX/GPIO5: now also TP41.P$1
- net UART-RX/GPIO6: now also TP48.P$1
- net UART-RX/GPIO7: now also TP55.P$1
- net UART-RX/GPIO8: now also TP62.P$1
- net UART-TX/GPIO1: now also TP12.P$1
- net UART-TX/GPIO2: now also TP19.P$1
- net UART-TX/GPIO3: now also TP26.P$1
- net UART-TX/GPIO4: now also TP33.P$1
- net UART-TX/GPIO48: now also TP5.P$1
- net UART-TX/GPIO5: now also TP40.P$1
- net UART-TX/GPIO6: now also TP47.P$1
- net UART-TX/GPIO7: now also TP54.P$1
- net UART-TX/GPIO8: now also TP61.P$1
- net VDCDCRF1: now also C34.1; no longer C33.1
- net VDCDCRF2: now also C62.1; no longer C60.1
- net VDCDCRF3: now also C90.1; no longer C87.1
- net VDCDCRF4: now also C118.1; no longer C114.1
- net VDCDCRF5: now also C146.1; no longer C141.1
- net VDCDCRF6: now also C174.1; no longer C168.1
- net VDCDCRF7: now also C202.1; no longer C195.1
- net VDCDCRF8: now also C230.1; no longer C222.1
- net VDD: no longer C11.1, U1.H3
- net VDD1: now also C44.1, C51.1, D9.C; no longer C38.1, C43.1, C46.1, D7.C, U5.H3
- net VDD2: now also C72.1, C78.1, C79.1, D15.C, D16.C; no longer C65.1, C66.1, C73.1, C74.1, D13.C, D14.C, U9.H3
- net VDD3: now also C105.1, C106.1, C107.1, C98.1, D22.C, D23.C; no longer C101.1, C102.1, C92.1, C93.1, C94.1, D19.C, D20.C, U13.H3
- net VDD4: now also C125.1, C126.1, C132.1, C133.1, C134.1, C135.1, D29.C, D30.C; no longer C119.1, C120.1, C121.1, C122.1, C127.1, C129.1, C130.1, D25.C, D26.C, U17.H3
- net VDD5: now also C152.1, C153.1, C159.1, C160.1, C161.1, C162.1, C163.1, D36.C, D37.C; no longer C146.1, C147.1, C148.1, C149.1, C150.1, C155.1, C157.1, C158.1, D31.C, D32.C, U21.H3
- net VDD6: now also C179.1, C180.1, C187.1, C188.1, C189.1, C190.1, C191.1, D43.C, D44.C; no longer C173.1, C174.1, C175.1, C176.1, C177.1, C178.1, C183.1, C185.1, D37.C, D38.C, U25.H3
- net VDD7: now also C207.1, C215.1, C216.1, C217.1, C218.1, C219.1, D50.C, D51.C; no longer C200.1, C201.1, C202.1, C203.1, C204.1, C205.1, C211.1, D43.C, D44.C, U29.H3
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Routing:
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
